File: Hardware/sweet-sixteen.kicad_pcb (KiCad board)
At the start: 2 copper layers, 116 x 105 mm, 83 parts, among them P1 SDA_I, P10 VIN_O, P11 GND_O, P12 SDA_O, P13 CLK_O, P14 LE_O, P15 ~OE_O, P2 CLK_I, P3 LE_I, P4 ~OE_I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

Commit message: add extra vias on VIN
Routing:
- net VIN: track 160.0 -> 162.0 mm, vias 6 -> 8
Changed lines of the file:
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@@
     (links 326)
     (no_connects 0)
-    (area 99.69481 49.949999 242.796801 155.050001)
+    (area 99.949999 49.949999 216.050001 155.050001)
     (thickness 1.6)
     (drawings 6)
-    (tracks 1597)
+    (tracks 1601)
     (zones 0)
     (modules 83)
@@
   )
   (setup
-    (last_trace_width 0.508)
+    (last_trace_width 2.54)
     (user_trace_width 0.254)
     (user_trace_width 0.508)
@@
   (segment (start 140.905 146.332302) (end 141.867467 147.294769) (width 0.254) (layer F.Cu) (net 147) (status 10))
   (segment (start 140.905 145.699) (end 140.905 146.1435) (width 0.254) (layer F.Cu) (net 147) (status 30))
+  (segment (start 200.5 64.5) (end 196 60) (width 2.54) (layer B.Cu) (net 148))
+  (segment (start 201.5 65.5) (end 200.5 64.5) (width 2.54) (layer B.Cu) (net 148))
+  (via (at 200.5 64.5) (size 0.6) (drill 0.4) (layers F.Cu B.Cu) (net 148))
+  (segment (start 105 60) (end 105 62) (width 2.54) (layer B.Cu) (net 148))
+  (via (at 105 62) (size 0.6) (drill 0.4) (layers F.Cu B.Cu) (net 148))
   (segment (start 195 57.5) (end 195.754 57.5) (width 0.254) (layer F.Cu) (net 148) (status 10))
   (segment (start 195.754 57.5) (end 199 60.746) (width 0.254) (layer F.Cu) (net 148))
@@
   (segment (start 105 62) (end 101.5 65.5) (width 2.54) (layer F.Cu) (net 148) (status 20))
   (via (at 105 60) (size 0.6) (drill 0.4) (layers F.Cu B.Cu) (net 148))
-  (segment (start 201.5 65.5) (end 196 60) (width 2.54) (layer B.Cu) (net 148))
   (segment (start 214.5 65.5) (end 203 65.5) (width 2.54) (layer F.Cu) (net 148) (status 10))
   (segment (start 203 65.5) (end 201.5 65.5) (width 2.54) (layer F.Cu) (net 148))

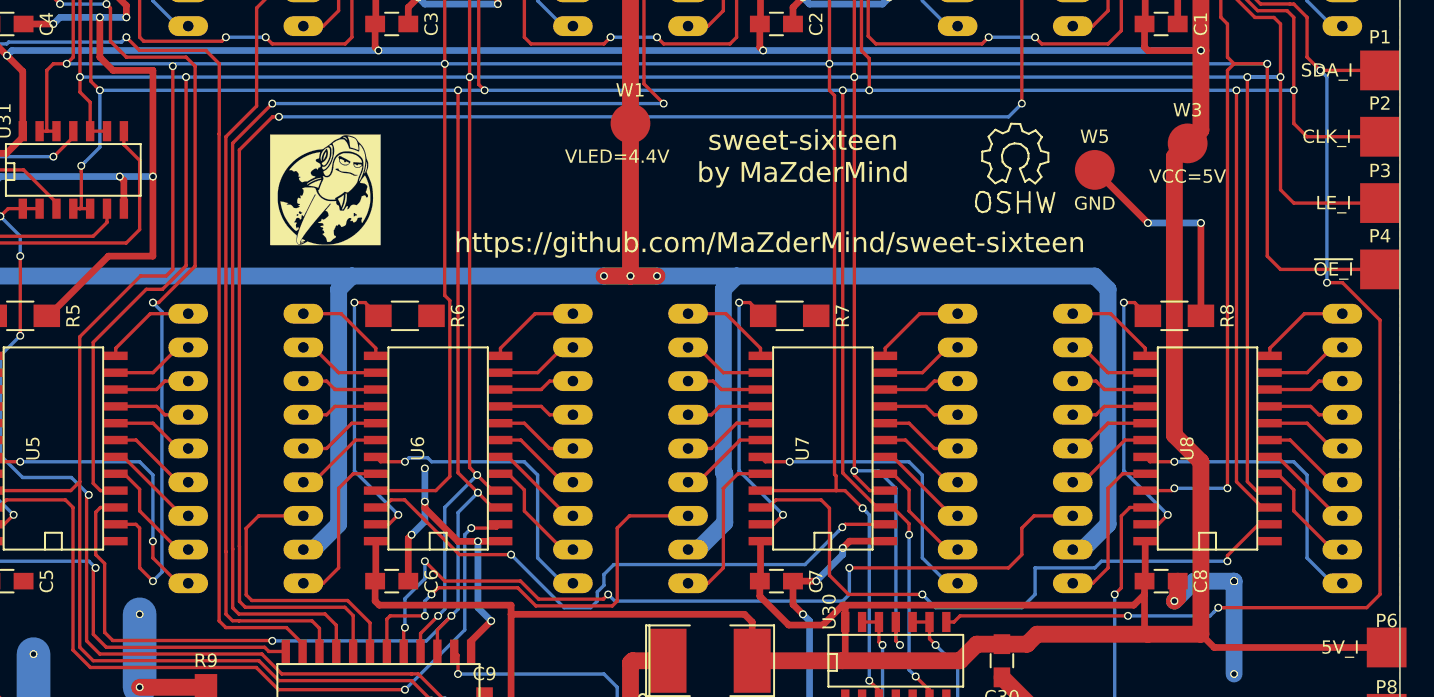
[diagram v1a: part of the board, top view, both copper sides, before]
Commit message: remove wrong gnd pin on pi connecor, add some labels
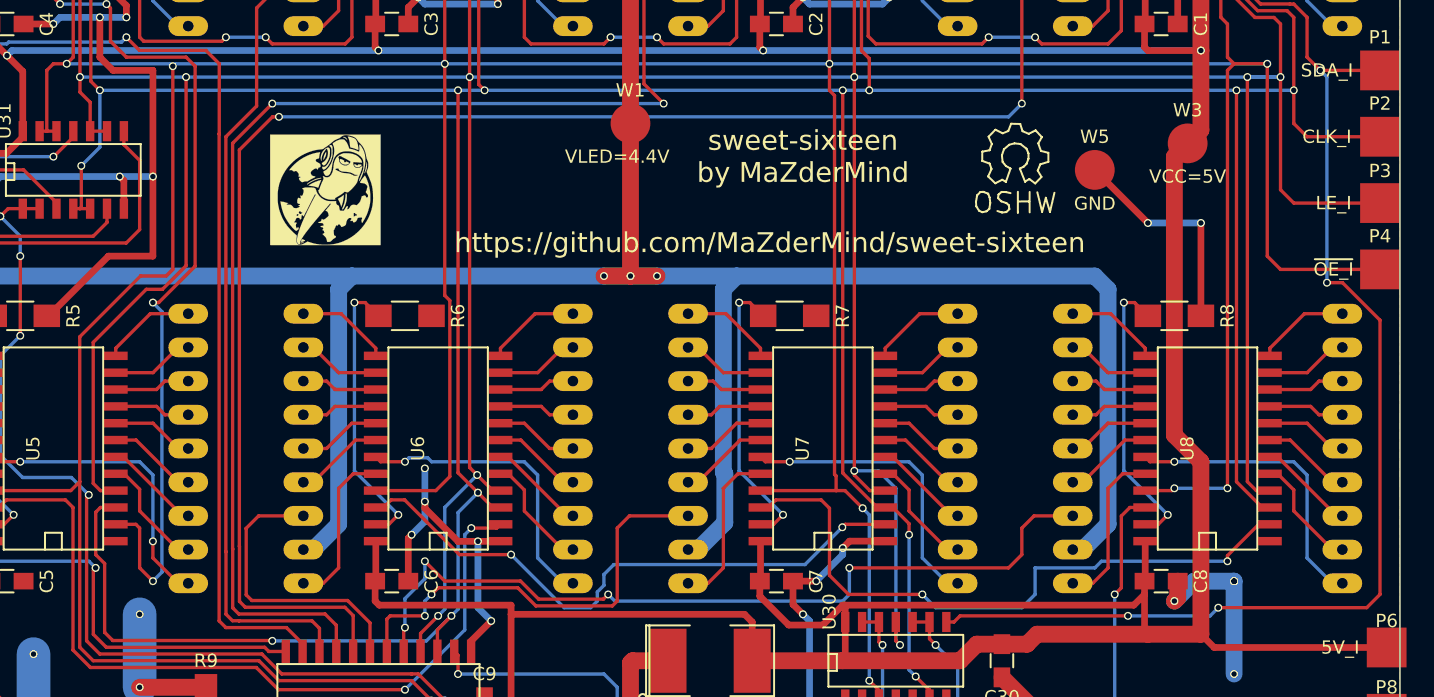
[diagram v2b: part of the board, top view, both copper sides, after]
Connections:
- P5 pad 35: GND -> (no net)

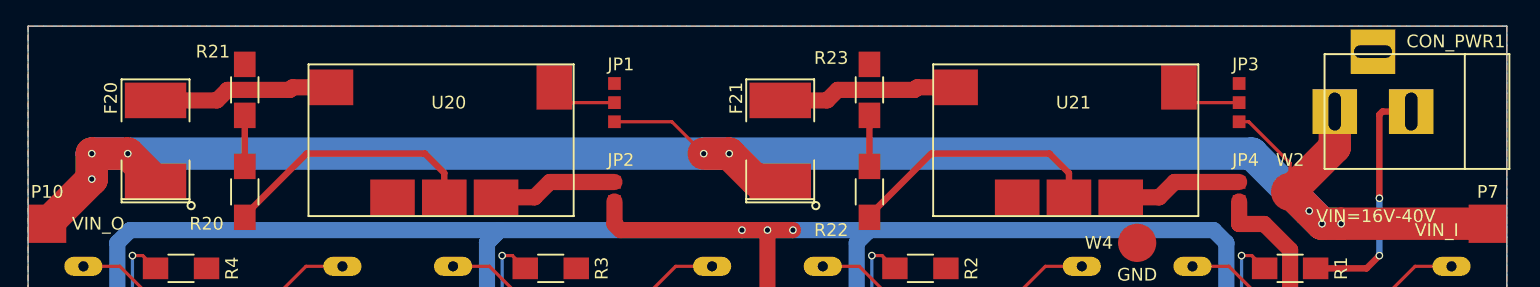
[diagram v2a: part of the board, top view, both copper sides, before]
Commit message: add 2.5M mounting holes to the top of the pcb
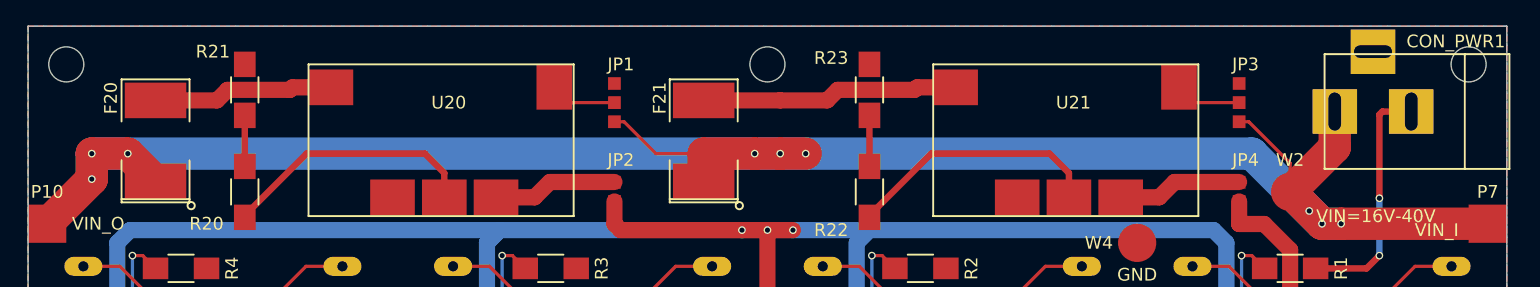
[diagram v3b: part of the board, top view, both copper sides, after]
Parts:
- added ?: M2.5, rpi-header:m25-mounting-hole, F.Cu at (158.0, 53.0)
- added ?: M2.5, rpi-header:m25-mounting-hole, F.Cu at (213.0, 53.0)
- added ?: M2.5, rpi-header:m25-mounting-hole, F.Cu at (103.0, 53.0)
- moved F21 6.00 mm to (153.0, 59.0)
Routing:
- net Net-(F21-Pad2): track 14.2 -> 20.2 mm
- net VIN: track 162.0 -> 165.2 mm, vias 8 -> 9
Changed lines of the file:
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@@
     (thickness 1.6)
     (drawings 6)
-    (tracks 1594)
+    (tracks 1600)
     (zones 0)
-    (modules 83)
+    (modules 86)
     (nets 190)
   )
@@
   )
   (setup
-    (last_trace_width 2.54)
+    (last_trace_width 0.254)
     (user_trace_width 0.254)
     (user_trace_width 0.508)
@@
     (mod_text_size 1 1)
     (mod_text_width 0.15)
-    (pad_size 5 5)
-    (pad_drill 3.1)
+    (pad_size 2.75 2.75)
+    (pad_drill 2.75)
     (pad_to_mask_clearance 0.254)
     (solder_mask_min_width 0.1524)
@@
     (add_net VIN)
   )
+  (module rpi-header:m25-mounting-hole (layer F.Cu)
+    (at 158 53)
+    (fp_text reference "" (at 0 0.5) (layer F.SilkS)
+      (effects (font (size 1 1) (thickness 0.15)))
+    )
+    (fp_text value M2.5 (at 0 -2.54) (layer F.Fab)
+      (effects (font (size 1 1) (thickness 0.15)))
+    )
+    (pad "" np_thru_hole circle (at 0 0) (size 2.75 2.75) (drill 2.75) (layers *.Cu *.Mask F.SilkS))
+  )
+  (module rpi-header:m25-mounting-hole (layer F.Cu)
+    (at 213 53)
+    (fp_text reference "" (at 0 0.5) (layer F.SilkS)
+      (effects (font (size 1 1) (thickness 0.15)))
+    )
+    (fp_text value M2.5 (at 0 -2.54) (layer F.Fab)
+      (effects (font (size 1 1) (thickness 0.15)))
+    )
+    (pad "" np_thru_hole circle (at 0 0) (size 2.75 2.75) (drill 2.75) (layers *.Cu *.Mask F.SilkS))
+  )
   (module chips:STP16CPC26MTR locked (layer F.Cu)
     (at 201.5 79 90)
@@
   )
   (module SMD_Packages:SMD-2112_Pol (layer F.Cu)
-    (at 159 59 90)
+    (at 153 59 90)
     (attr smd)
     (fp_text reference F21 (at 3.355 -3.45 270) (layer F.SilkS)
@@
     )
   )
+  (module rpi-header:m25-mounting-hole (layer F.Cu)
+    (at 103 53)
+    (fp_text reference "" (at 0 0.5) (layer F.SilkS)
+      (effects (font (size 1 1) (thickness 0.15)))
+    )
+    (fp_text value M2.5 (at 0 -2.54) (layer F.Fab)
+      (effects (font (size 1 1) (thickness 0.15)))
+    )
+    (pad "" np_thru_hole circle (at 0 0) (size 2.75 2.75) (drill 2.75) (layers *.Cu *.Mask F.SilkS))
+  )
   (gr_text https://github.com/MaZderMind/sweet-sixteen (at 168.5 105.5) (layer F.SilkS)
     (effects (font (size 1.5 1.5) (thickness 0.3)))
@@
   (segment (start 140.905 146.332302) (end 141.867467 147.294769) (width 0.254) (layer F.Cu) (net 147) (status 10))
   (segment (start 140.905 145.699) (end 140.905 146.1435) (width 0.254) (layer F.Cu) (net 147) (status 30))
+  (segment (start 146 57.5) (end 146.754 57.5) (width 0.254) (layer F.Cu) (net 148))
+  (segment (start 146.754 57.5) (end 149.254 60) (width 0.254) (layer F.Cu) (net 148))
+  (segment (start 149.254 60) (end 153 60) (width 0.254) (layer F.Cu) (net 148))
+  (segment (start 196 60) (end 161 60) (width 2.54) (layer B.Cu) (net 148))
+  (segment (start 161 60) (end 159 60) (width 2.54) (layer B.Cu) (net 148))
+  (segment (start 159 60) (end 161 60) (width 2.54) (layer F.Cu) (net 148))
+  (via (at 161 60) (size 0.6) (drill 0.4) (layers F.Cu B.Cu) (net 148))
+  (segment (start 159 60) (end 155 60) (width 2.54) (layer B.Cu) (net 148))
+  (segment (start 157 60) (end 159 60) (width 2.54) (layer F.Cu) (net 148))
+  (via (at 159 60) (size 0.6) (drill 0.4) (layers F.Cu B.Cu) (net 148))
+  (segment (start 153 60) (end 157 60) (width 2.54) (layer F.Cu) (net 148))
+  (via (at 157 60) (size 0.6) (drill 0.4) (layers F.Cu B.Cu) (net 148))
+  (segment (start 153 62.175) (end 153 60) (width 2.54) (layer F.Cu) (net 148))
   (segment (start 200.5 64.5) (end 196 60) (width 2.54) (layer B.Cu) (net 148))
   (segment (start 201.5 65.5) (end 200.5 64.5) (width 2.54) (layer B.Cu) (net 148))
@@
   (segment (start 195.754 57.5) (end 199 60.746) (width 0.254) (layer F.Cu) (net 148))
   (segment (start 199 60.746) (end 199 63) (width 0.254) (layer F.Cu) (net 148) (status 20))
-  (segment (start 146 57.5) (end 150.5 57.5) (width 0.254) (layer F.Cu) (net 148) (status 10))
-  (segment (start 150.5 57.5) (end 153 60) (width 0.254) (layer F.Cu) (net 148))
   (segment (start 105 60) (end 107.825 60) (width 2.54) (layer F.Cu) (net 148))
   (via (at 107.825 60) (size 0.6) (drill 0.4) (layers F.Cu B.Cu) (net 148))
@@
   (segment (start 155 60) (end 153 60) (width 2.54) (layer B.Cu) (net 148))
   (segment (start 153 60) (end 105 60) (width 2.54) (layer B.Cu) (net 148))
-  (segment (start 155 60) (end 153 60) (width 2.54) (layer F.Cu) (net 148))
-  (via (at 153 60) (size 0.6) (drill 0.4) (layers F.Cu B.Cu) (net 148))
-  (segment (start 196 60) (end 155 60) (width 2.54) (layer B.Cu) (net 148))
-  (segment (start 157.175 62.175) (end 155 60) (width 2.54) (layer F.Cu) (net 148) (status 10))
-  (via (at 155 60) (size 0.6) (drill 0.4) (layers F.Cu B.Cu) (net 148))
-  (segment (start 159 62.175) (end 157.175 62.175) (width 2.54) (layer F.Cu) (net 148) (status 30))
   (segment (start 105 60) (end 105 62) (width 2.54) (layer F.Cu) (net 148))
   (segment (start 105 62) (end 101.5 65.5) (width 2.54) (layer F.Cu) (net 148) (status 20))
@@
   (segment (start 110 55.825) (end 114.821998 55.825) (width 1.27) (layer F.Cu) (net 170) (status 10))
   (segment (start 114.821998 55.825) (end 115.646998 55) (width 1.27) (layer F.Cu) (net 170))
+  (segment (start 159 55.825) (end 153 55.825) (width 1.27) (layer F.Cu) (net 171))
   (segment (start 163.508 55) (end 169.54 55) (width 1.27) (layer F.Cu) (net 171))
   (segment (start 169.54 55) (end 169.74 54.8) (width 1.27) (layer F.Cu) (net 171))

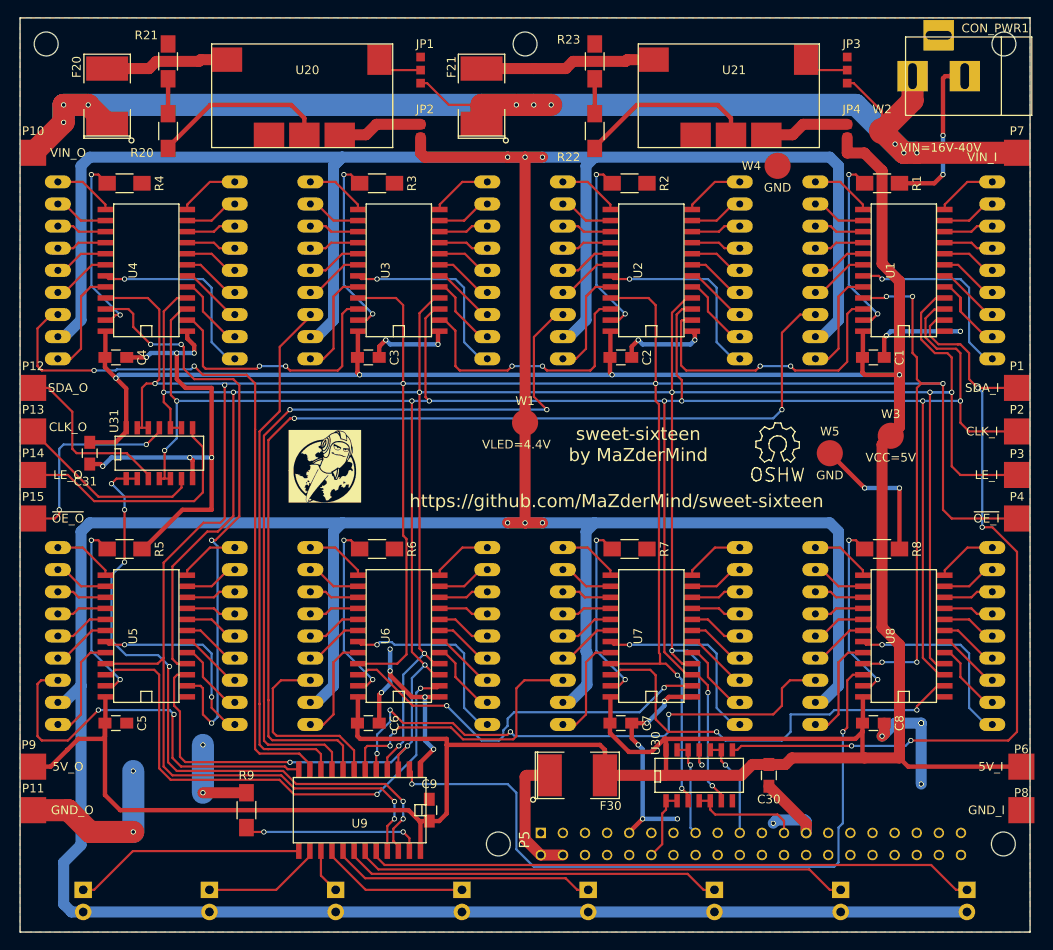
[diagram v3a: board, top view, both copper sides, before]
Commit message: clean up BOM, add Button
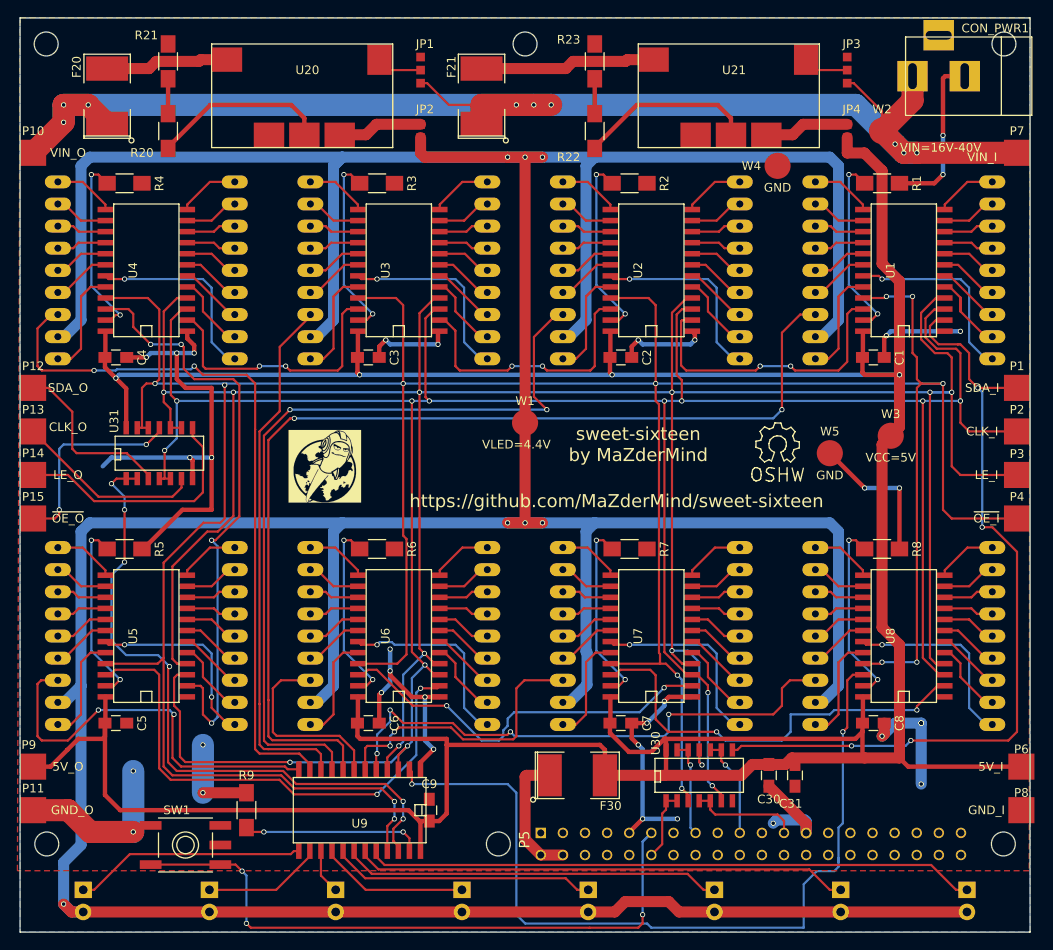
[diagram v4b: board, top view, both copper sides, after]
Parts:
- added ?: M2.5, rpi-header:m25-mounting-hole, F.Cu at (212.9, 144.9)
- added SW1: SW_PUSH, ADTSM61:ADTSM61, F.Cu at (119.0, 145.0)
- C1, C2, C3, C30, C4, C5, C6, C7, C8, C9: value 10nf -> 0.1μF
- C31: value 100nf -> 0.1μF
- moved C31 89.1 mm to (189.0, 137.0)
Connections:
- P5 pad 11: (no net) -> Net-(P5-Pad11)
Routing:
- net Net-(P5-Pad11): track 0.00 -> 75.1 mm, vias 0 -> 3
- net /SDA_89: track 82.2 -> 96.1 mm
- net VCC: track 412.6 -> 407.9 mm
- net /VLED: track 544.6 -> 548.2 mm, vias 6 -> 7
- net GND: track 234.8 -> 233.2 mm, vias 36 -> 35
